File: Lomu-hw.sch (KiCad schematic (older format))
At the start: 1 part

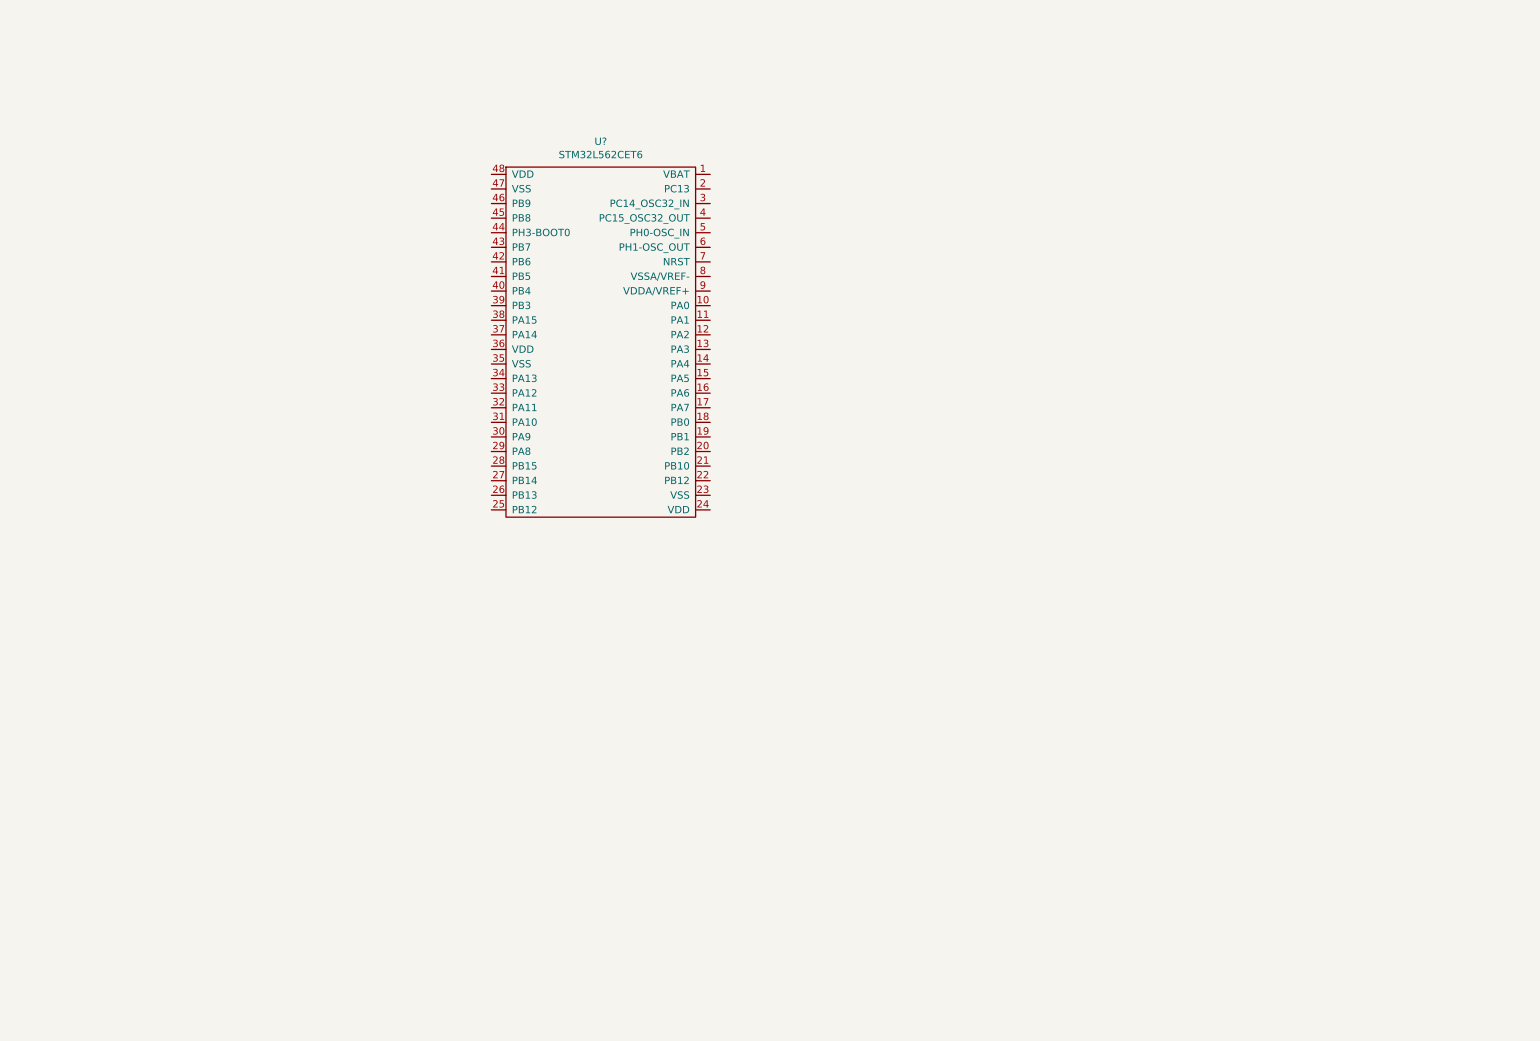
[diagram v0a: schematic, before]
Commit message: Updates project from mPCIe F1 template
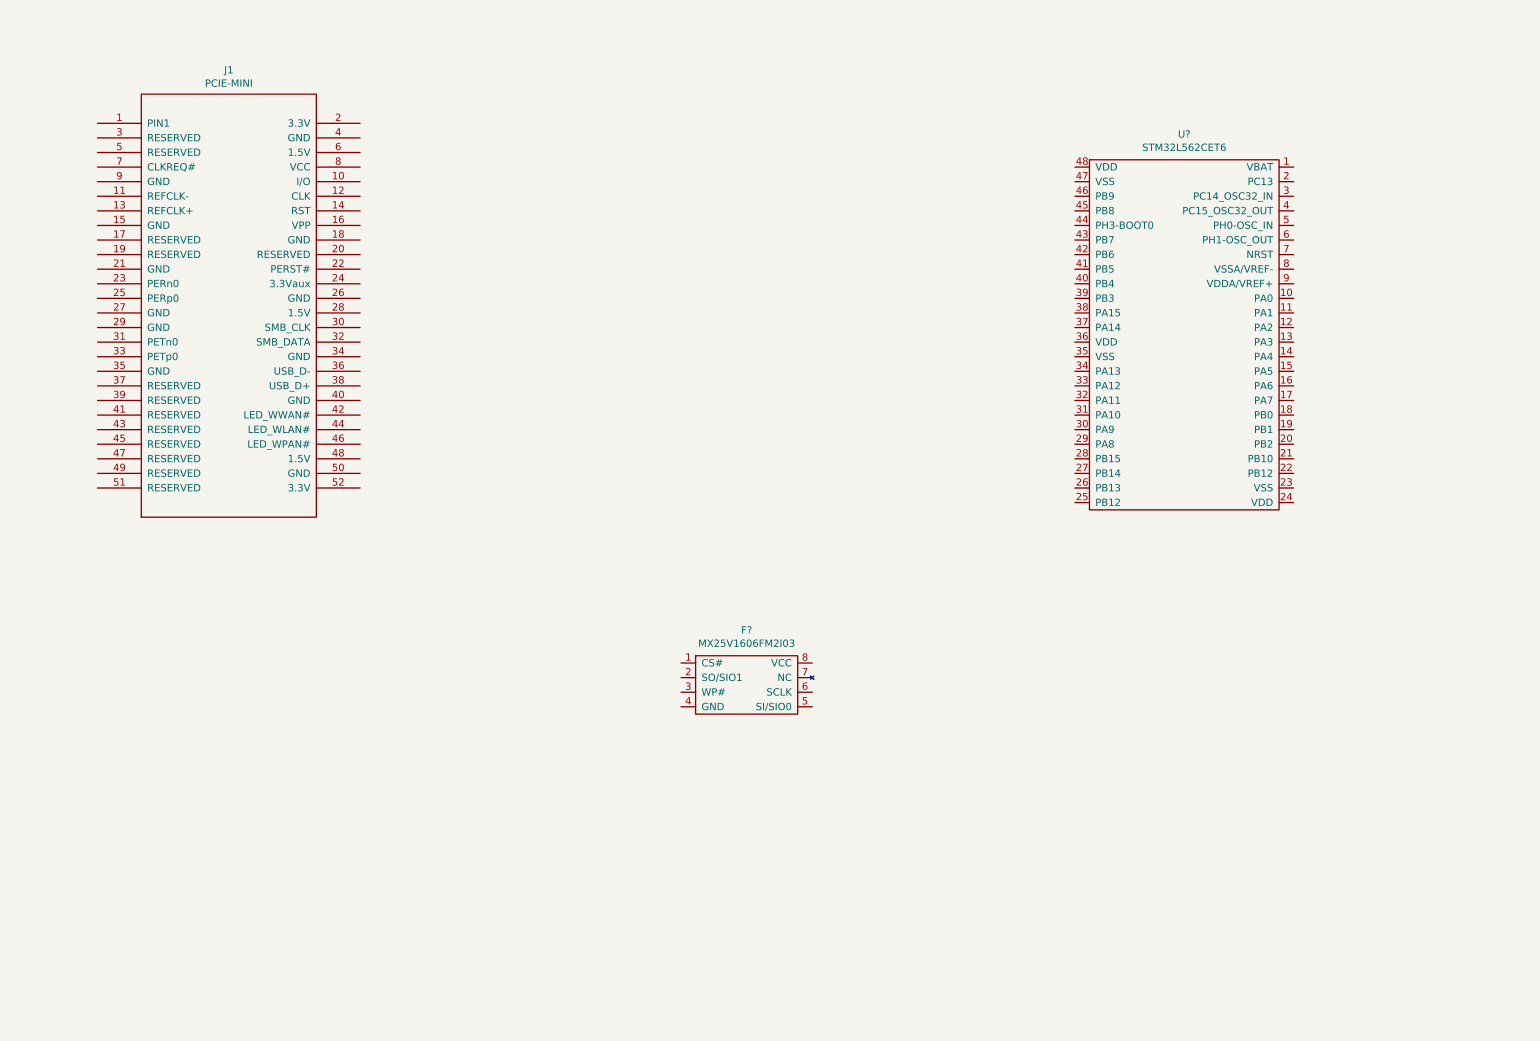
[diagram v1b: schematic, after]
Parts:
- removed U?: STM32L562CET6, symbol lomu:STM32L562CET6
- added F?: MX25V1606FM2I03, symbol lomu:MX25V1606FM2I03
- added J1: PCIE-MINI, mini-PCIe:miniPCIeConn, symbol mini-PCIe:PCIE-MINI
- added U?: STM32L562CET6, symbol lomu:STM32L562CET6
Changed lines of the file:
@@
 $EndDescr
 $Comp
-L lomu:STM32L562CET6 U?
-U 1 1 6027D55A
-P 4650 1650
-F 0 "U?" H 4650 1725 50  0000 C CNN
-F 1 "STM32L562CET6" H 4650 1634 50  0000 C CNN
-F 2 "" H 4650 1650 50  0001 C CNN
-F 3 "" H 4650 1650 50  0001 C CNN
-	1    4650 1650
+L mini-PCIe:PCIE-MINI J1
+U 1 1 602A6AB9
+P 2100 2700
+F 0 "J1" H 2100 4315 50  0000 C CNN
+F 1 "PCIE-MINI" H 2100 4224 50  0000 C CNN
+F 2 "mini-PCIe:miniPCIeConn" H 2100 2700 50  0001 C CNN
+F 3 "DOCUMENTATION" H 2100 1300 50  0001 C CNN
+	1    2100 2700
 	1    0    0    -1
 $EndComp
+$Comp
+L lomu:STM32L562CET6 U?
+U 1 1 602D2AFD
+P 8650 1600
+F 0 "U?" H 8650 1675 50  0000 C CNN
+F 1 "STM32L562CET6" H 8650 1584 50  0000 C CNN
+F 2 "" H 8650 1600 50  0001 C CNN
+F 3 "" H 8650 1600 50  0001 C CNN
+	1    8650 1600
+	1    0    0    -1
+$EndComp
+$Comp
+L lomu:MX25V1606FM2I03 F?
+U 1 1 602D3910
+P 5650 5000
+F 0 "F?" H 5650 5075 50  0000 C CNN
+F 1 "MX25V1606FM2I03" H 5650 4984 50  0000 C CNN
+F 2 "" H 5650 5000 50  0001 C CNN
+F 3 "" H 5650 5000 50  0001 C CNN
+	1    5650 5000
+	1    0    0    -1
+$EndComp

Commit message: Adds crystals and LED
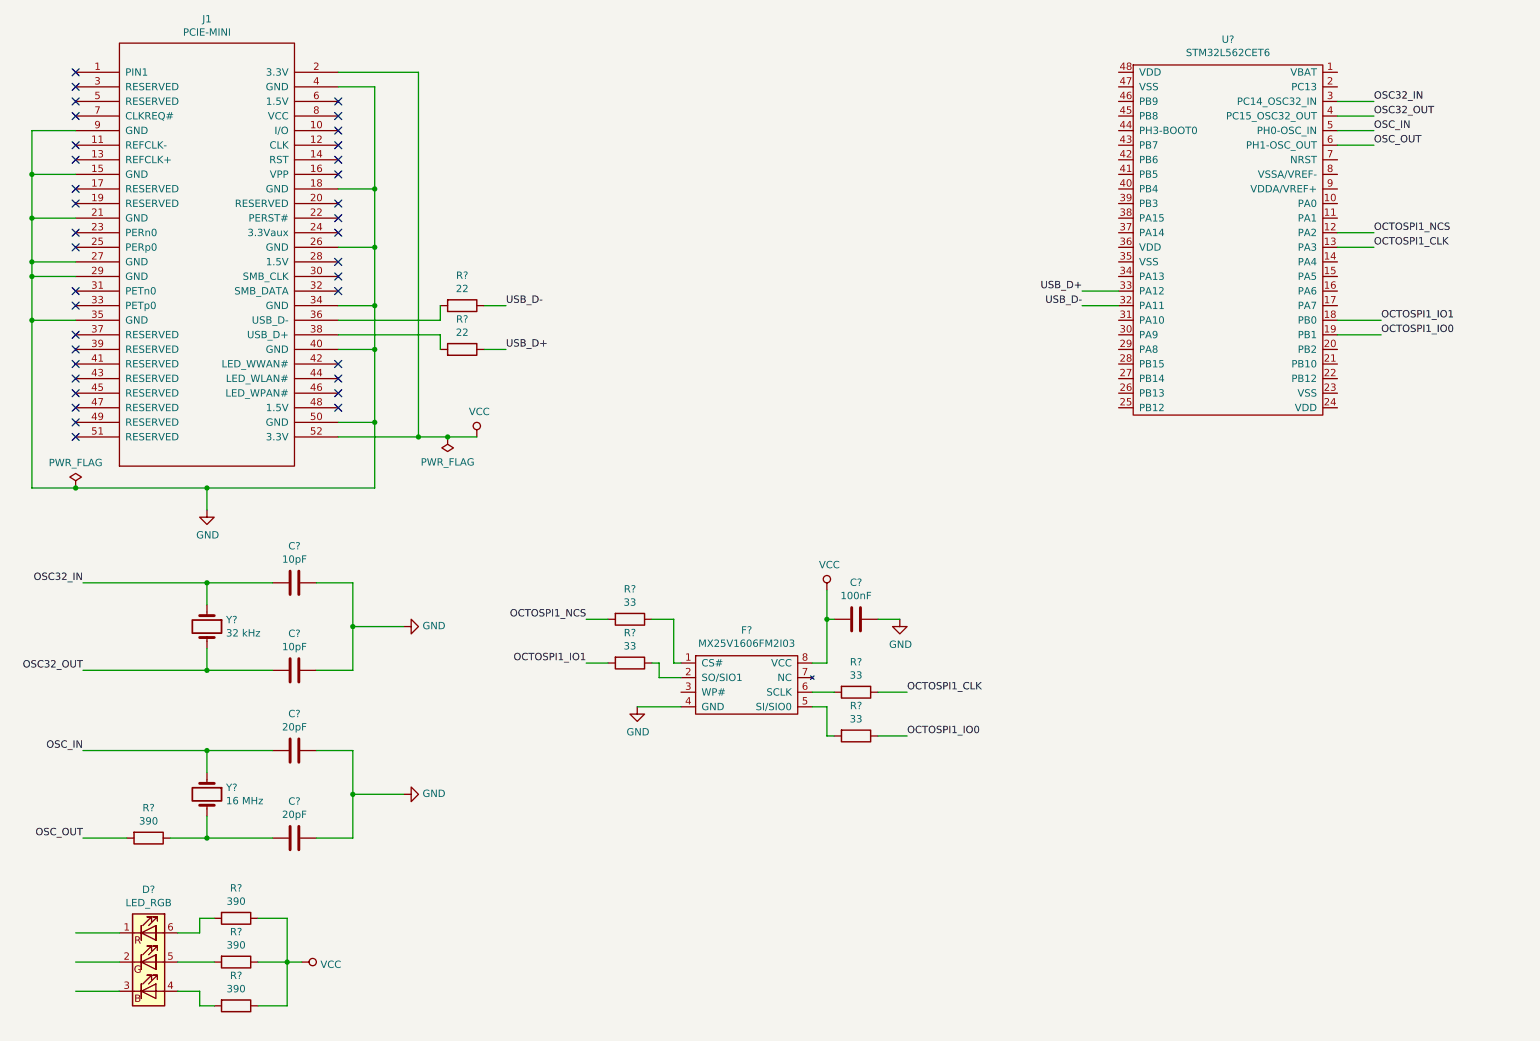
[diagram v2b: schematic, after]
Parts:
- added C? (x2): 20pF, symbol Device:C
- added C? (x2): 10pF, symbol Device:C
- added C?: 100nF, symbol Device:C
- added D?: LED_RGB, symbol Device:LED_RGB
- added R? (x4): 390, symbol Device:R
- added R? (x2): 22, symbol Device:R
- added R? (x4): 33, symbol Device:R
- added Y?: 16 MHz, symbol Device:Crystal
- added Y?: 32 kHz, symbol Device:Crystal
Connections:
- net labels added: GND, OCTOSPI1_CLK, OCTOSPI1_IO0, OCTOSPI1_IO1, OCTOSPI1_NCS, OSC32_IN, OSC32_OUT, OSC_IN, OSC_OUT, USB_D+, USB_D-, VCC
- wire segments 0 -> 108
- no-connect marks 0 -> 36
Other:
- moved on the sheet: J1, U?

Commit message: Adds remaining components
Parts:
- added C? (x7): 100nF, symbol Device:C
- added C?: 4.7uF, symbol Device:C
- added C?: 47pF, symbol Device:C
- added H? (x2): MountingHole_Pad, symbol Mechanical:MountingHole_Pad
- added J?: ARM_SWD_6, symbol lomu:ARM_SWD_6
- added R?: 10k, symbol Device:R
- added SW?: SW_Push_Dual, symbol Switch:SW_Push_Dual
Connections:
- net labels added: LED1, LED2, LED3, NRST, TCK_SWCLK, TDO_SWO, TMS_SWDIO
- wire segments 108 -> 193
- no-connect marks 36 -> 58
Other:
- moved on the sheet: C?, F?, R?

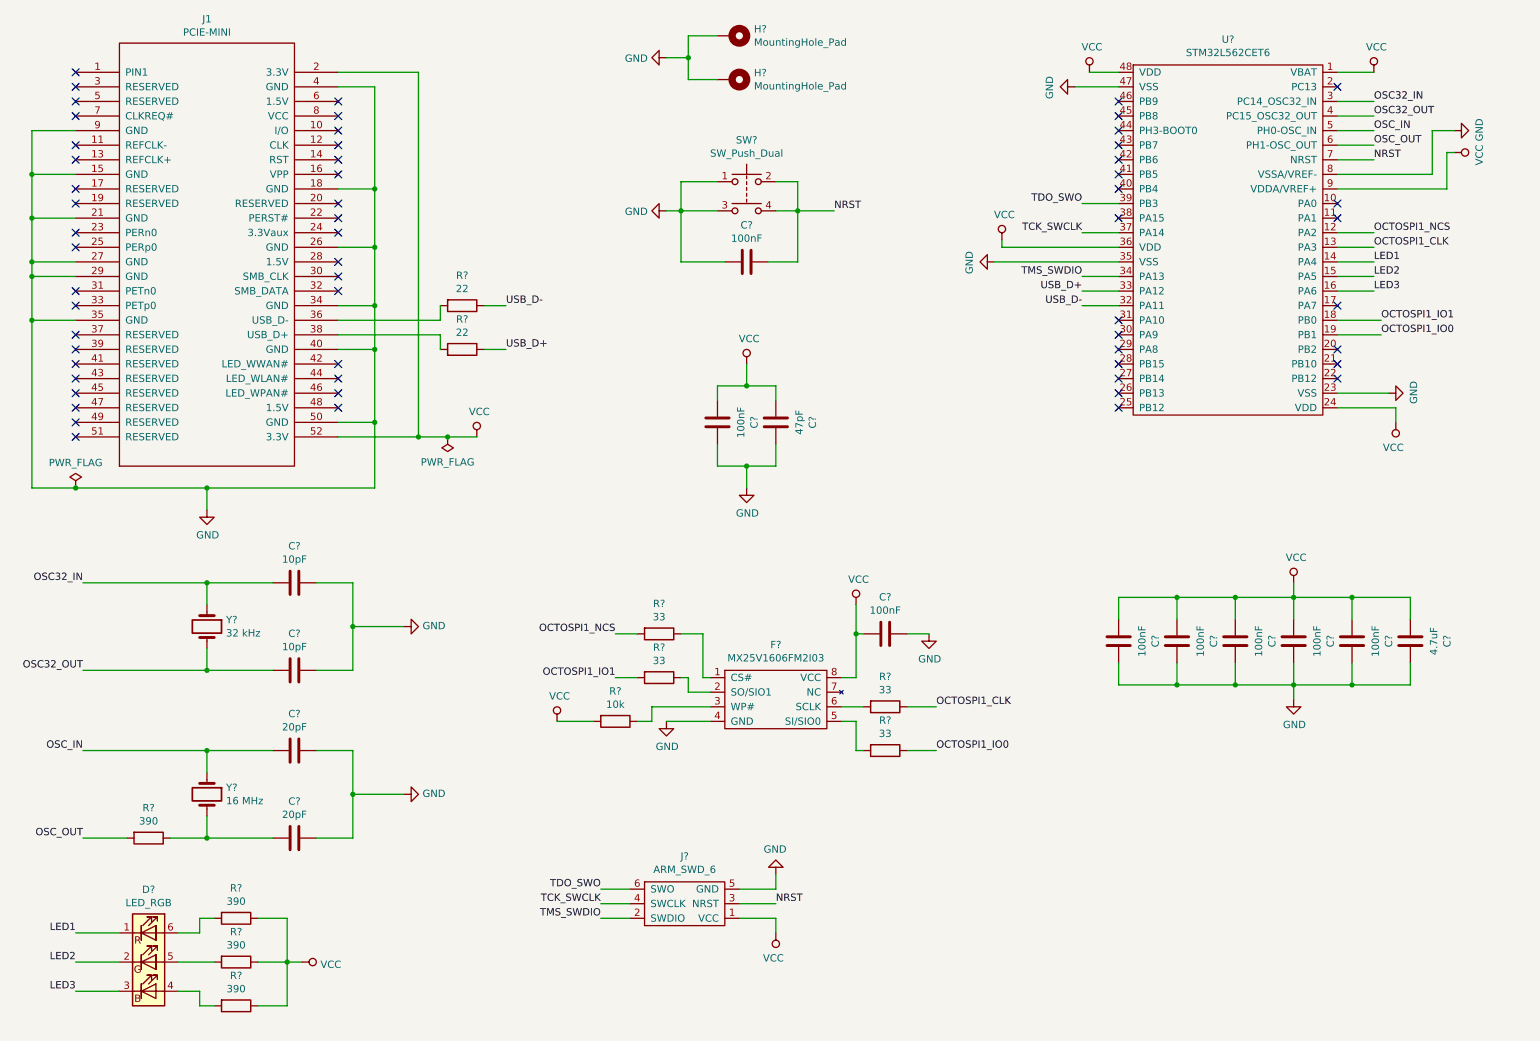
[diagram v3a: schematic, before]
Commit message: Adds first draft of layout
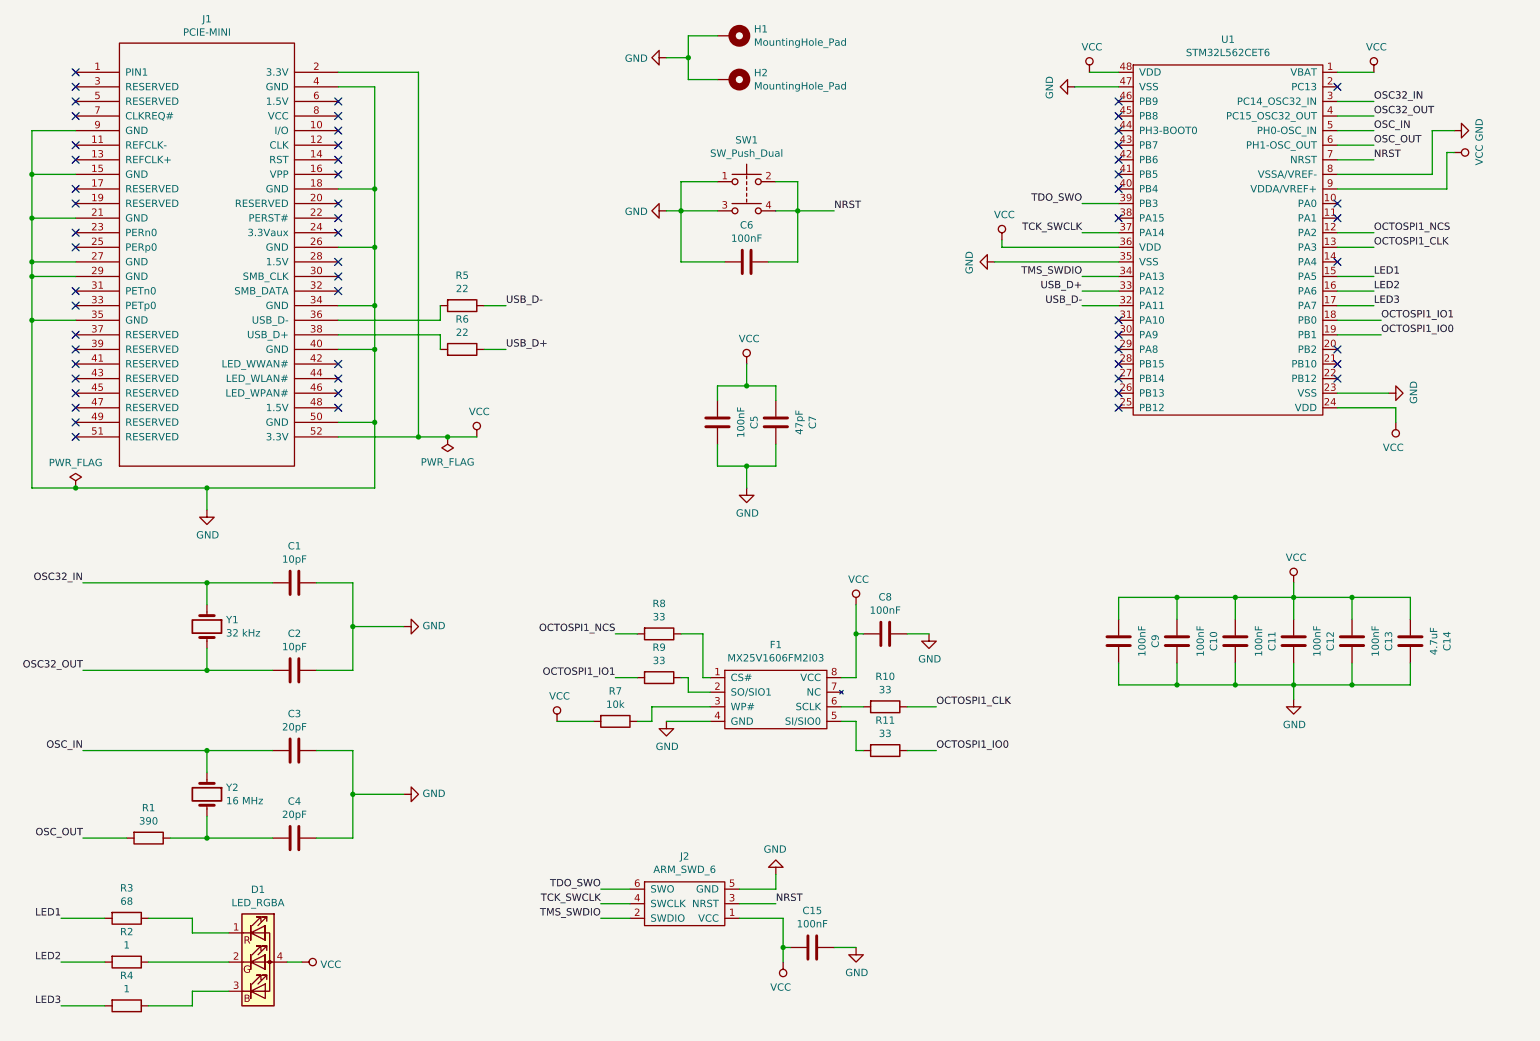
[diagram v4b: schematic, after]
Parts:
- removed D?: LED_RGB, symbol Device:LED_RGB
- added C15: 100nF, Capacitor_SMD:C_0805_2012Metric_Pad1.15x1.40mm_HandSolder, symbol Device:C
- added D1: LED_RGBA, LED_SMD:LED_RGB_1210, symbol Device:LED_RGBA
- C1, C2, C3, C4, C7: renamed from C?; footprint (none) -> Capacitor_SMD:C_0603_1608Metric_Pad1.05x0.95mm_HandSolder
- C10, C11, C12, C13, C14, C5, C6, C8, C9: renamed from C?; footprint (none) -> Capacitor_SMD:C_0805_2012Metric_Pad1.15x1.40mm_HandSolder
- F1: renamed from F?; footprint (none) -> Package_SO:SOP-8_5.28x5.23mm_P1.27mm
- H1, H2: renamed from H?; footprint (none) -> MountingHole:MountingHole_2.5mm_Pad
- J2: renamed from J?; footprint (none) -> Connector_PinHeader_1.27mm:PinHeader_2x03_P1.27mm_Vertical_SMD
- R1, R10, R11, R5, R6, R7, R8, R9: renamed from R?; footprint (none) -> Resistor_SMD:R_0805_2012Metric_Pad1.15x1.40mm_HandSolder
- R2, R4: renamed from R?; value 390 -> 1; footprint (none) -> Resistor_SMD:R_0805_2012Metric_Pad1.15x1.40mm_HandSolder
- R3: renamed from R?; value 390 -> 68; footprint (none) -> Resistor_SMD:R_0805_2012Metric_Pad1.15x1.40mm_HandSolder
- SW1: renamed from SW?; footprint (none) -> Button_Switch_SMD:SW_Push_1P1T_NO_6x6mm_H9.5mm
- U1: renamed from U?; footprint (none) -> Package_QFP:LQFP-48_7x7mm_P0.5mm
- Y1: renamed from Y?; footprint (none) -> Crystal:Crystal_SMD_3215-2Pin_3.2x1.5mm
- Y2: renamed from Y?; footprint (none) -> Crystal:Crystal_SMD_3225-4Pin_3.2x2.5mm_HandSoldering
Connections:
- net GND: now also C15.1
- net LED1: now also R3.2, U1.15 (PA5); no longer U1.14 (PA4)
- net LED2: now also R2.2, U1.16 (PA6); no longer U1.15 (PA5)
- net LED3: now also R4.2, U1.17 (PA7); no longer U1.16 (PA6)
- net VCC: now also C15.2, D1.4 (A); no longer R2.1, R3.1, R4.1
- new net: D1.2 (GK), R2.1
- new net: D1.1 (RK), R3.1
- new net: D1.3 (BK), R4.1
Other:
- moved on the sheet: R2, R3, R4

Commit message: Adds missing boot select trace
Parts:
- added R12: 10k, Resistor_SMD:R_0805_2012Metric_Pad1.15x1.40mm_HandSolder, symbol Device:R
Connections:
- net GND: now also R12.2
- net at U1.44 (PH3-BOOT0): now also R12.1
- no-connect marks 58 -> 57
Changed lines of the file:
@@
-$EndComp
-$Comp
-L power:GND #PWR0114
-U 1 1 603A961B
-P 7900 1200
-F 0 "#PWR0114" H 7900 950 50  0001 C CNN
-F 1 "GND" H 7905 1027 50  0000 C CNN
-F 2 "" H 7900 1200 50  0001 C CNN
-F 3 "" H 7900 1200 50  0001 C CNN
-	1    7900 1200
-	0    1    1    0
 $EndComp
 $Comp
@@
 $EndComp
 Wire Wire Line
-	8200 1200 7900 1200
-Wire Wire Line
 	8200 2400 7350 2400
 Wire Wire Line
@@
 NoConn ~ 8200 1300
 NoConn ~ 8200 1400
-NoConn ~ 8200 1500
 NoConn ~ 8200 1600
 NoConn ~ 8200 1700
@@
 Wire Wire Line
 	1550 7500 1850 7500
+Wire Wire Line
+	8200 1200 7900 1200
+$Comp
+L power:GND #PWR0114
+U 1 1 603A961B
+P 7900 1200
+F 0 "#PWR0114" H 7900 950 50  0001 C CNN
+F 1 "GND" H 7905 1027 50  0000 C CNN
+F 2 "" H 7900 1200 50  0001 C CNN
+F 3 "" H 7900 1200 50  0001 C CNN
+	1    7900 1200
+	0    1    1    0
+$EndComp
+$Comp
+L power:GND #PWR0127
+U 1 1 60D23205
+P 7650 1500
+F 0 "#PWR0127" H 7650 1250 50  0001 C CNN
+F 1 "GND" H 7655 1327 50  0000 C CNN
+F 2 "" H 7650 1500 50  0001 C CNN
+F 3 "" H 7650 1500 50  0001 C CNN
+	1    7650 1500
+	0    1    1    0
+$EndComp
+Wire Wire Line
+	7800 1500 7650 1500
+Wire Wire Line
+	8200 1500 8100 1500
+$Comp
+L Device:R R12
+U 1 1 60D3A664
+P 7950 1500
+F 0 "R12" V 7743 1500 50  0000 C CNN
+F 1 "10k" V 7834 1500 50  0000 C CNN
+F 2 "Resistor_SMD:R_0805_2012Metric_Pad1.15x1.40mm_HandSolder" V 7880 1500 50  0001 C CNN
+F 3 "~" H 7950 1500 50  0001 C CNN
+	1    7950 1500
+	0    1    1    0
+$EndComp
 $EndSCHEMATC

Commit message: Updates PDF
The PDF plot is now in sync again with the schematic
and includes the missing boot select trace and pull
down resistor.
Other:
- note added: "2021/06/22"
- note added: "v1.1"
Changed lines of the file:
@@
 	0    1    1    0
 $EndComp
+Text Notes 10800 7650 0    50   ~ 0
+v1.1
+Text Notes 8200 7650 0    50   ~ 0
+2021/06/22
 $EndSCHEMATC
